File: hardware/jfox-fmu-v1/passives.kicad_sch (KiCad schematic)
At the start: 39 parts, among them X1 16MHz, X2 32.768kHz

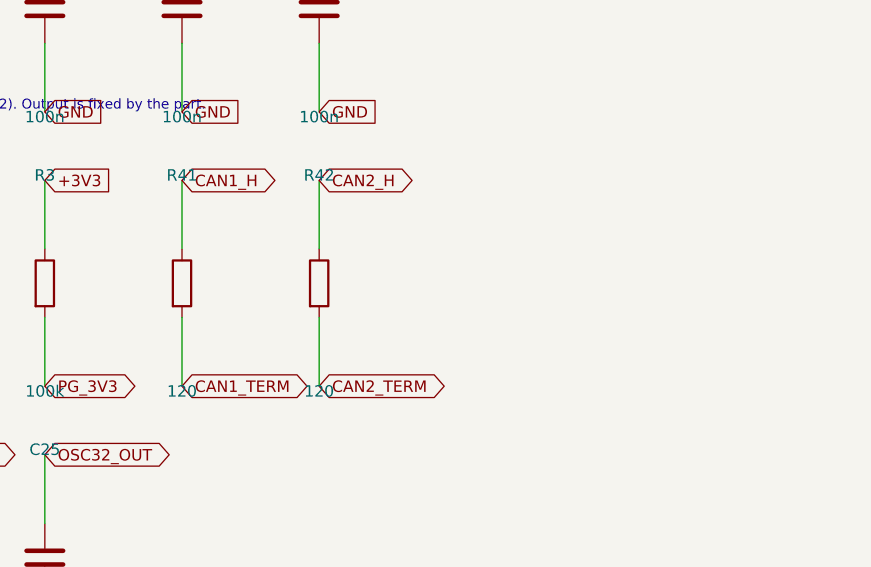
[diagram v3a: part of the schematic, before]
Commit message: Add the two sensors the design said it had
ARCHITECTURE.md specifies two barometers from two vendors and an internal
magnetometer. The schematic had one barometer and no magnetometer, and had had
neither for the whole life of the board. Every check passed the entire time.

That is the interesting part. The datasheet checks ask "is this part wired the
way its datasheet says", and all of them can pass on a board that is wired
perfectly and is still the wrong board. The nets for the missing sensors
existed - MAG_DRDY and BARO2_INT, correctly named, allocated to real MCU pins,
going nowhere - and "isolated label" is such ordinary ERC noise that sixty of
them hid two absent sensors.

U7 ICP-20100 (TDK) and U6 BMM150 (Bosch), both on I2C1, both from the
datasheets rather than from memory:

  ICP-20100  DS-000416 rev 1.3. Pinout table 18, strapping from figure 10's
             I2C typical circuit: CSB to VDDIO selects I2C, AD0 low gives
             0x63, pins 8 and 9 are "Connect to Ground" and are typed
             power_in so ERC objects if they float.
  BMM150     BST-BMM150-DS001-05 rev 1.4 table 32 and section 4.1: PS to
             VDDIO for reliable protocol selection, CSB and SDO both low for
             the default 0x10.

Addresses checked against each other rather than assumed: 0x10, 0x63, 0x76.
No collision on the shared bus.

R4/R5 4k7 pull-ups on I2C1. Both datasheets state outright that the bus needs
them; without them the line never releases and no sensor on it answers. The
board has had an I2C bus with no pull-ups since the day it was drawn.

The ICP-20100 footprint had to be drawn. It is the same 2x2 mm body and the
same ten pins as the BMP388 and a completely different land - Bosch puts three
pads left and right, TDK puts three top and bottom. Reusing the BMP388 land
would have placed ten pads that all landed somewhere and none on a terminal.

And the check that would have caught this in the first place:
check_fmu_objective.py encodes ARCHITECTURE.md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
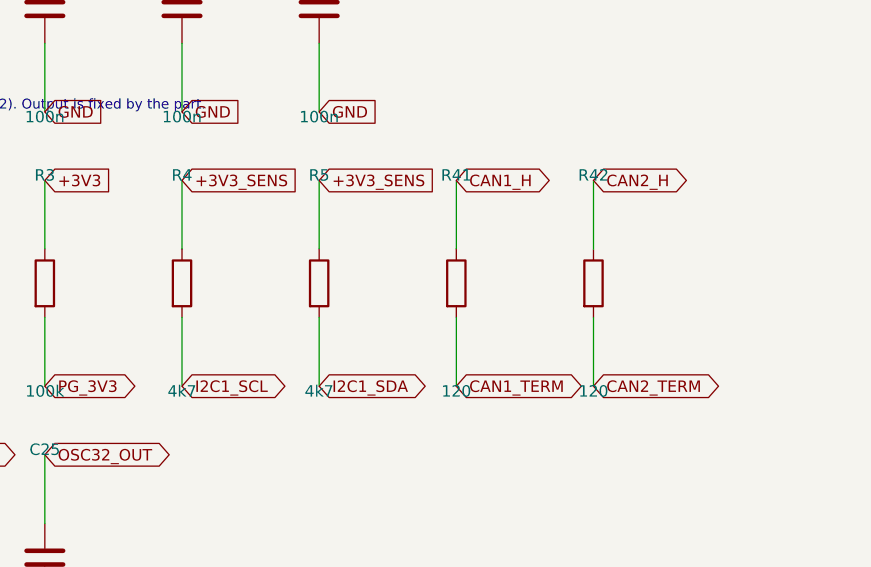
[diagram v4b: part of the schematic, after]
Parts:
- added R4, R5: 4k7, Resistor_SMD:R_0402_1005Metric, symbol Device:R
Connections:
- net +3V3_SENS: now also R4.1, R5.1
- new net I2C1_SCL: R4.2
- new net I2C1_SDA: R5.2

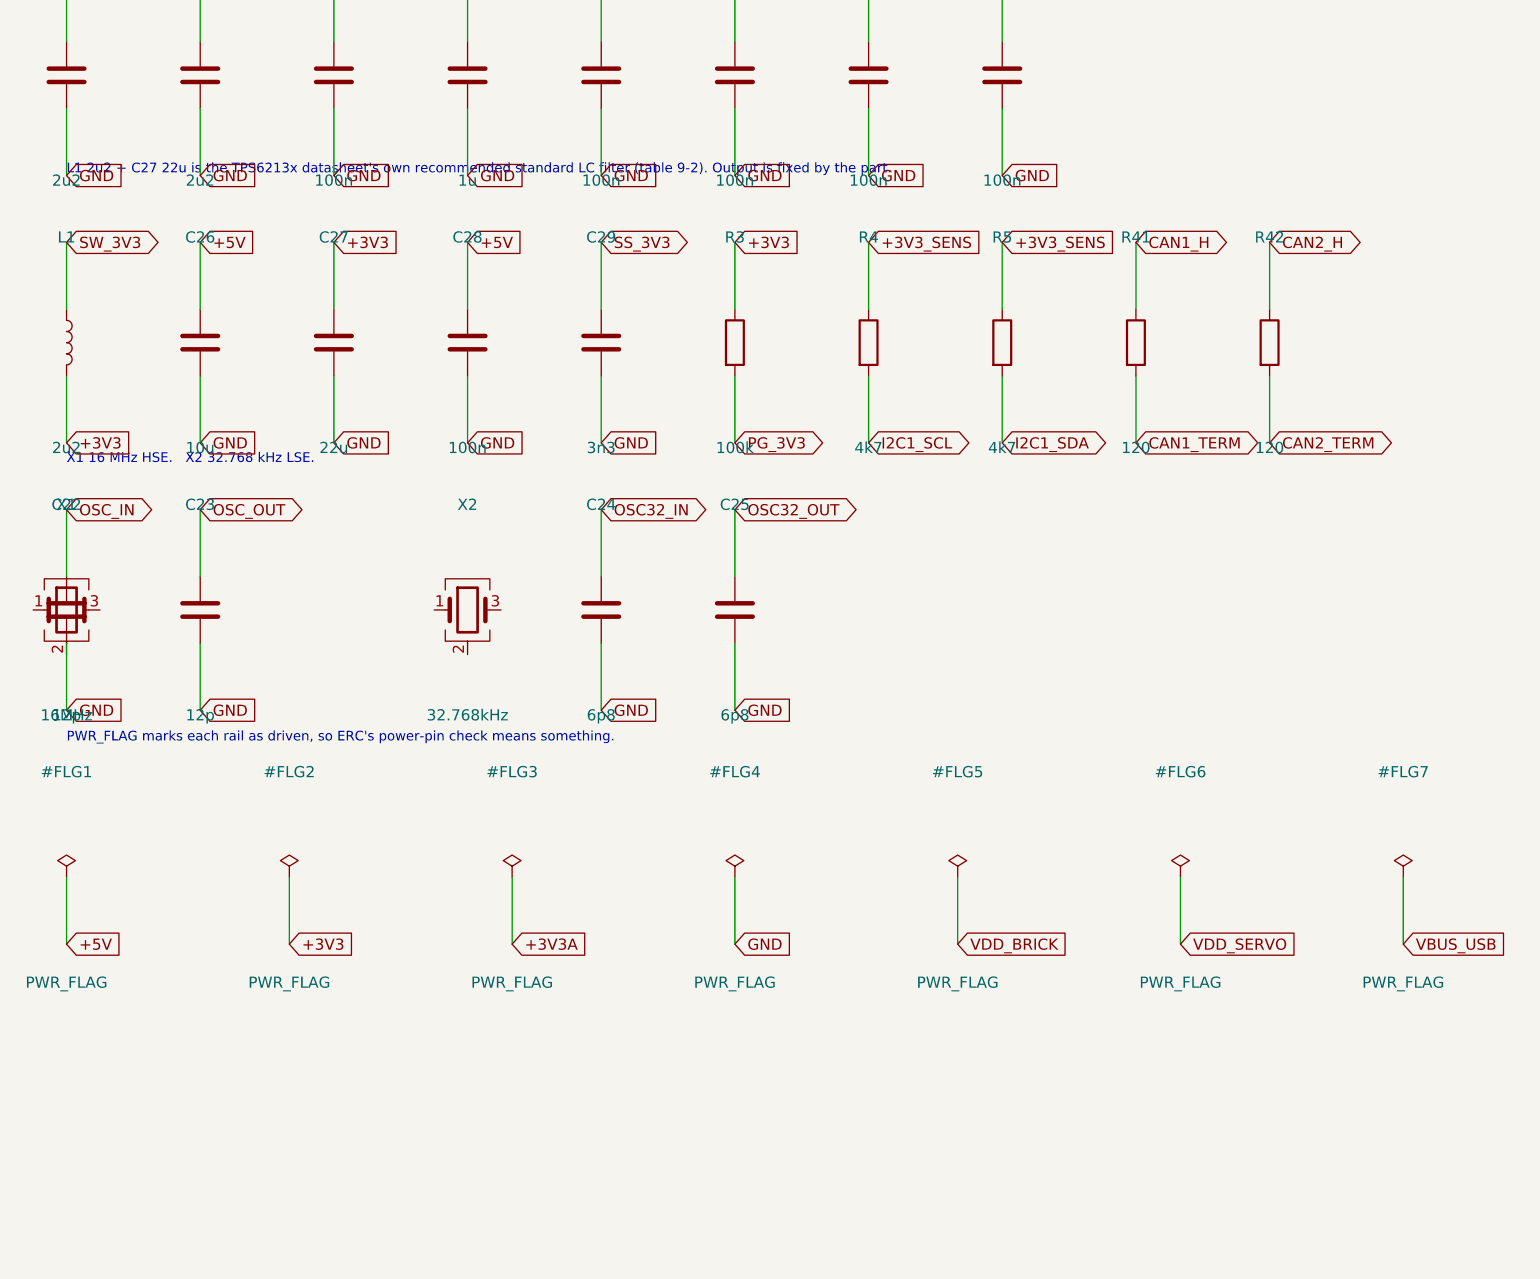
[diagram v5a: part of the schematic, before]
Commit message: The MCU power rail was drawn, not connected
Fourteen of the STM32H753's VDD pins were floating. The netlist put exactly
three U10 pins on +3V3: 6, 114 and 171 - the two pins at the ends of the rail
wire, plus PDR_ON on its own label. Everything between them was unconnected.

The cause is the fix from three commits ago. Joining same-net pins into a rail
was right; drawing a wire across their stub ends and stopping there was not.
KiCad does not connect a wire to another wire because one's endpoint lies on
it - crossings are crossings, and a T needs an explicit junction. The rail
therefore joined its own two endpoints and ran past the other fourteen taps.

It plots as an unmistakably connected power rail. It looked right in the PDF,
it looked right in the editor, and only the netlist disagreed. That is the
whole lesson: drawings can lie, netlists are what the board is made from.

The ground rail escaped by accident - the STM32 symbol stacks its VSS pins at
one location, so a single stub caught all thirteen. Had the VDD pins been
stacked too, this would have shipped.

gen_fmu_schematic now emits a junction at every intermediate tap.
check_fmu_schematic gains an eighth check that reads the PROJECT netlist and
asserts all 26 MCU supply pins land on their rail - and it had its own version
of the same mistake on the first run, reading the sensor sheet's netlist,
which does not contain U10 at all and so reported every pin missing on a
correct board. Negative-tested by stripping the 25 junctions back out: it
names all fourteen VDD pins and all twelve VSS pins.

Also added the reset circuit, which did not exist. NRST and BOOT0 were both
inputs with nothing driving them. NRST has an internal 30-50k pull-up
(DM00388325 s6.3.16 table 54) so it needs only the external capacitor from
figure 22; BOOT0 has no internal pull and gets 10k to ground, or a marginal
power-up can boot the system bootloader instead of flash.

Checked and NOT changed: VCAP1 and VCAP2 are tied. ERC flags it as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
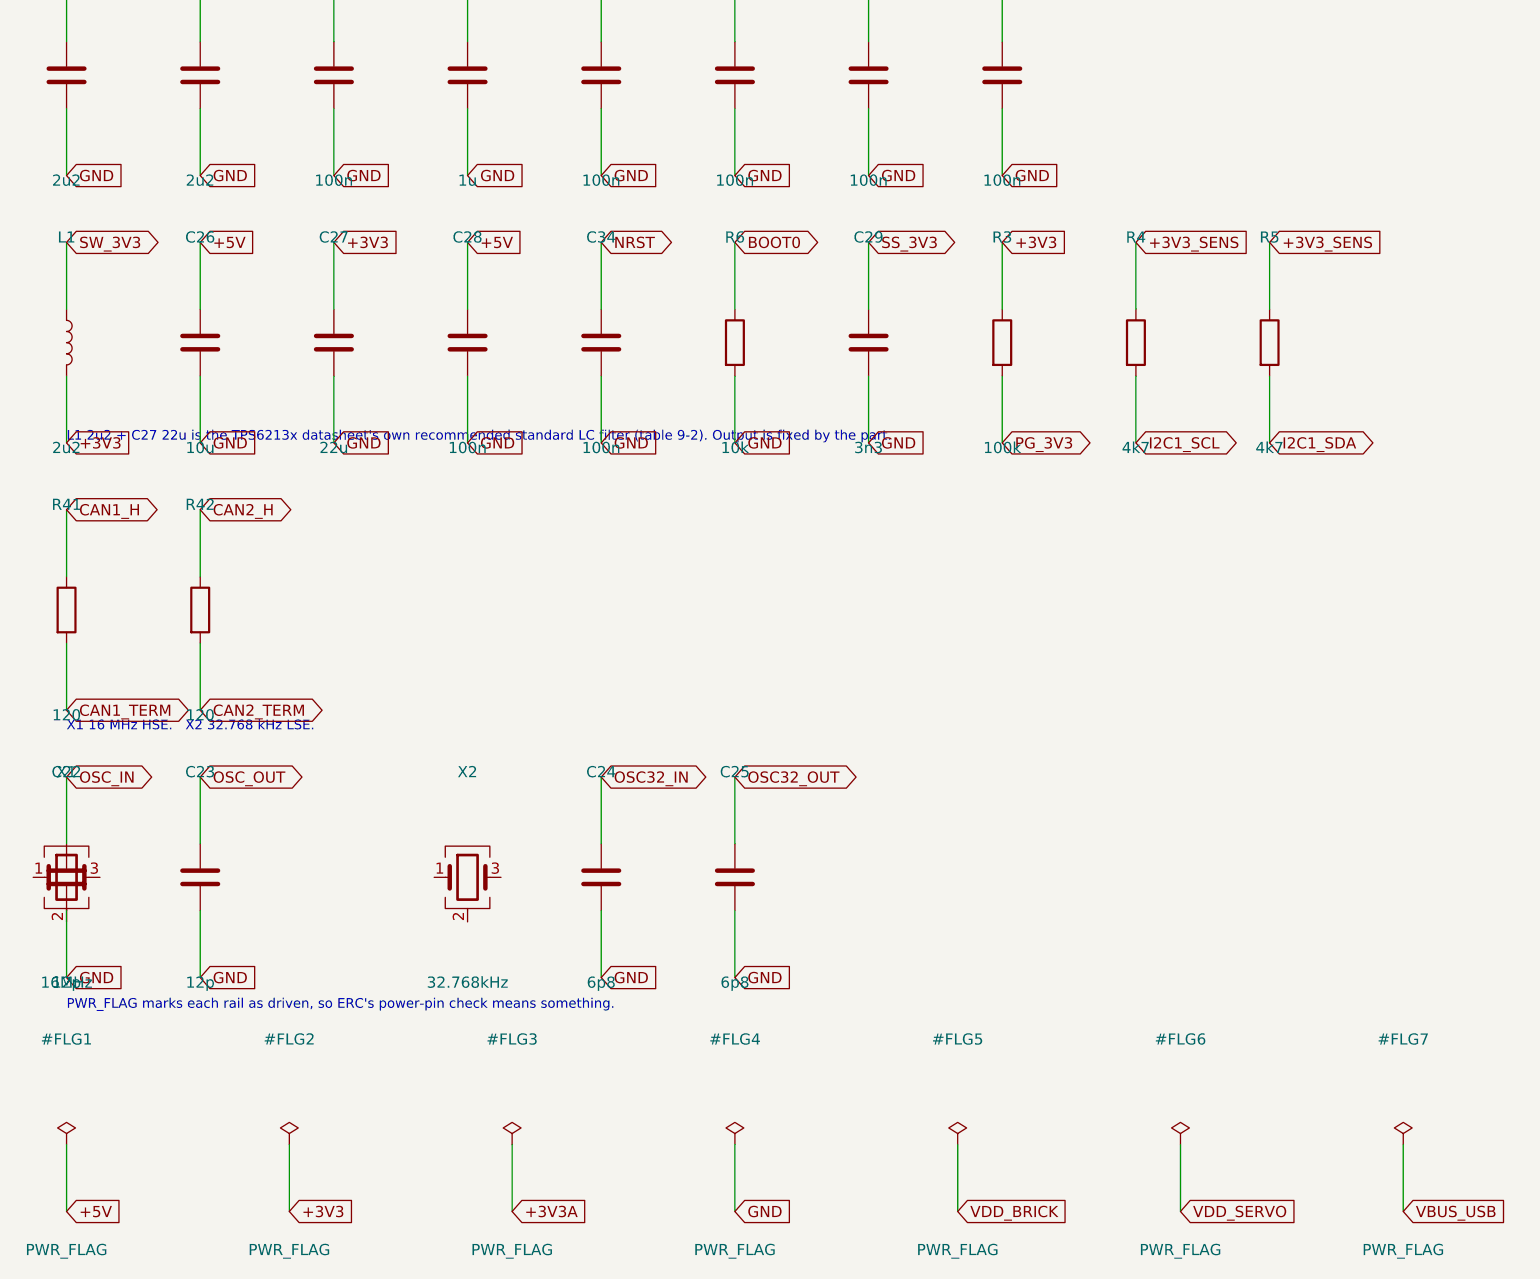
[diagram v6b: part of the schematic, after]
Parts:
- added C34: 100n, Capacitor_SMD:C_0402_1005Metric, symbol Device:C
- added R6: 10k, Resistor_SMD:R_0402_1005Metric, symbol Device:R
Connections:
- net GND: now also C34.2, R6.2
- new net BOOT0: R6.1
- new net NRST: C34.1
